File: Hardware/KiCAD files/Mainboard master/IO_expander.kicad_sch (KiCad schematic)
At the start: 7 parts

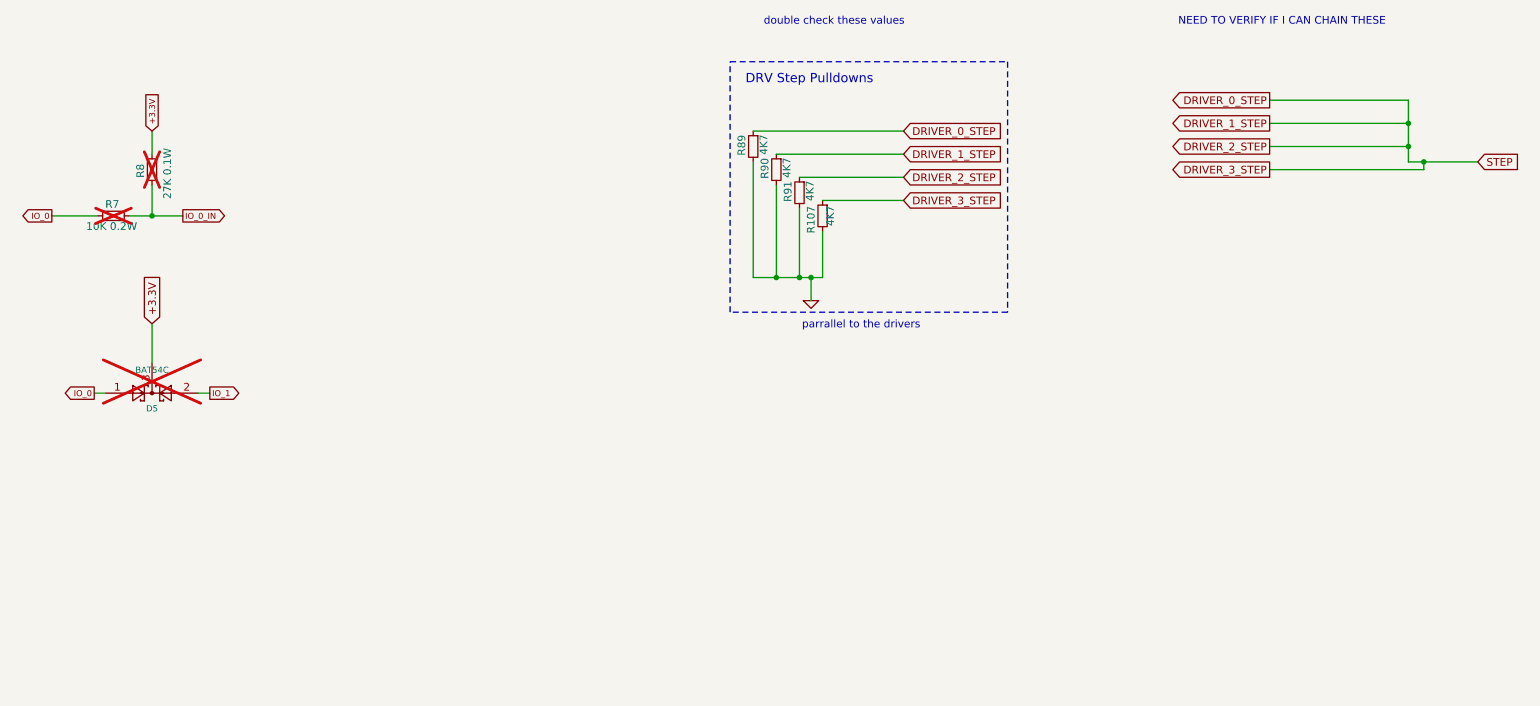
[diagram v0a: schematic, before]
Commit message: DRV 8825 and regulator purchased set
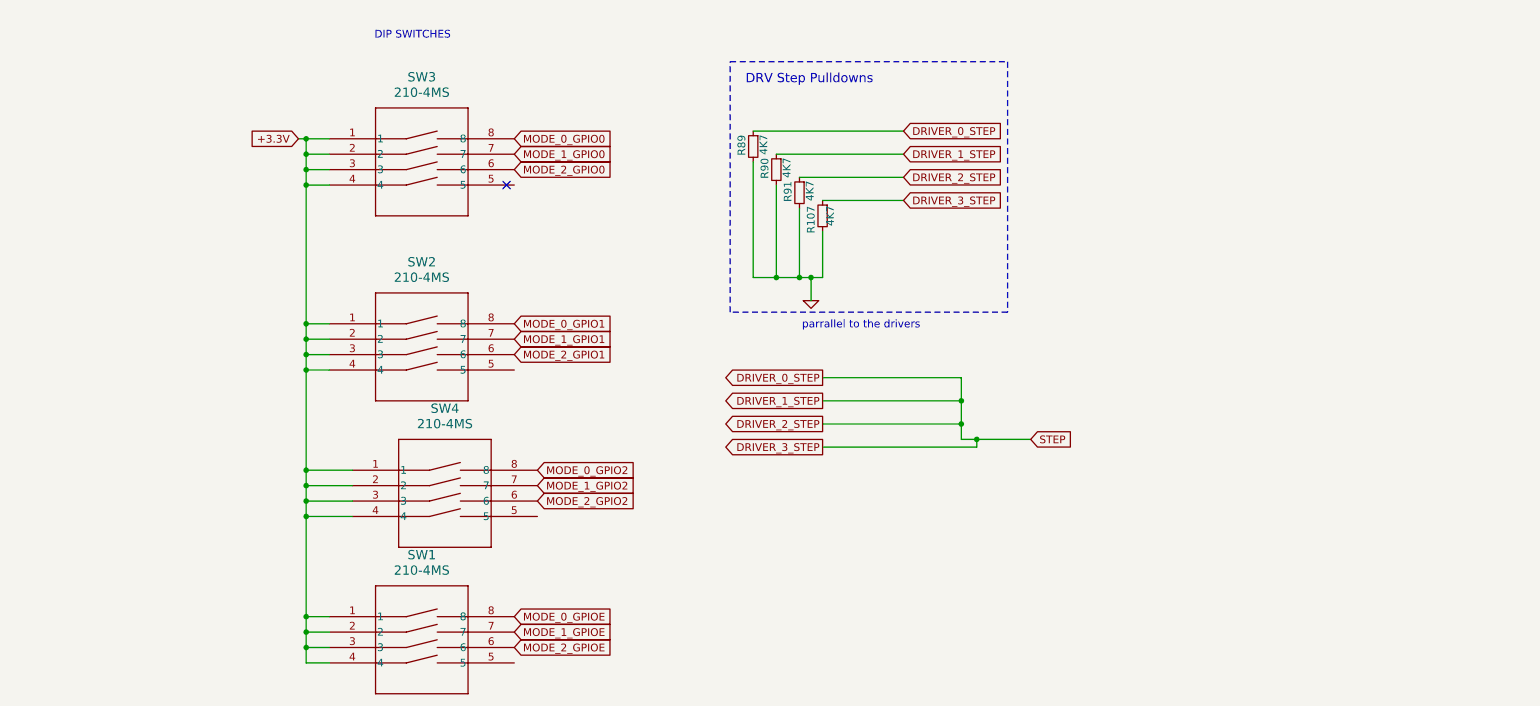
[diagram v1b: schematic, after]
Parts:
- removed D5: BAT54C, Package_TO_SOT_SMD:SOT-23, symbol Diode:BAT54C
- removed R7: 10K 0.2W, Resistor_SMD:R_0603_1608Metric_Wbry, symbol Device:R_Small
- removed R8: 27K 0.1W, Resistor_SMD:R_0402_1005Metric_Wbry, symbol Device:R_Small
- added SW1, SW2, SW3, SW4: 210-4MS, 4-pin DIP switch:DIP8_210-4_CTS, symbol 2026-04-21_02-24-22:210-4MS
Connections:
- net +3.3V: now also SW1.1, SW1.2, SW1.3, SW1.4, SW2.1, SW2.2, SW2.3, SW2.4, SW3.1, SW3.2, SW3.3, SW3.4, SW4.1, SW4.2, SW4.3, SW4.4
- new net MODE_0_GPIO0: SW3.8
- new net MODE_0_GPIO1: SW2.8
- new net MODE_0_GPIO2: SW4.8
- new net MODE_0_GPIOE: SW1.8
- new net MODE_1_GPIO0: SW3.7
- new net MODE_1_GPIO1: SW2.7
- new net MODE_1_GPIO2: SW4.7
- new net MODE_1_GPIOE: SW1.7
- new net MODE_2_GPIO0: SW3.6
- new net MODE_2_GPIO1: SW2.6
- new net MODE_2_GPIO2: SW4.6
- new net MODE_2_GPIOE: SW1.6
- no-connect marks 0 -> 1
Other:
- note added: "DIP SWITCHES"
- note removed: "NEED TO VERIFY IF I CAN CHAIN THESE"
- note removed: "double check these values"
